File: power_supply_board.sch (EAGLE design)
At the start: 30 parts, among them J6 1744426-2

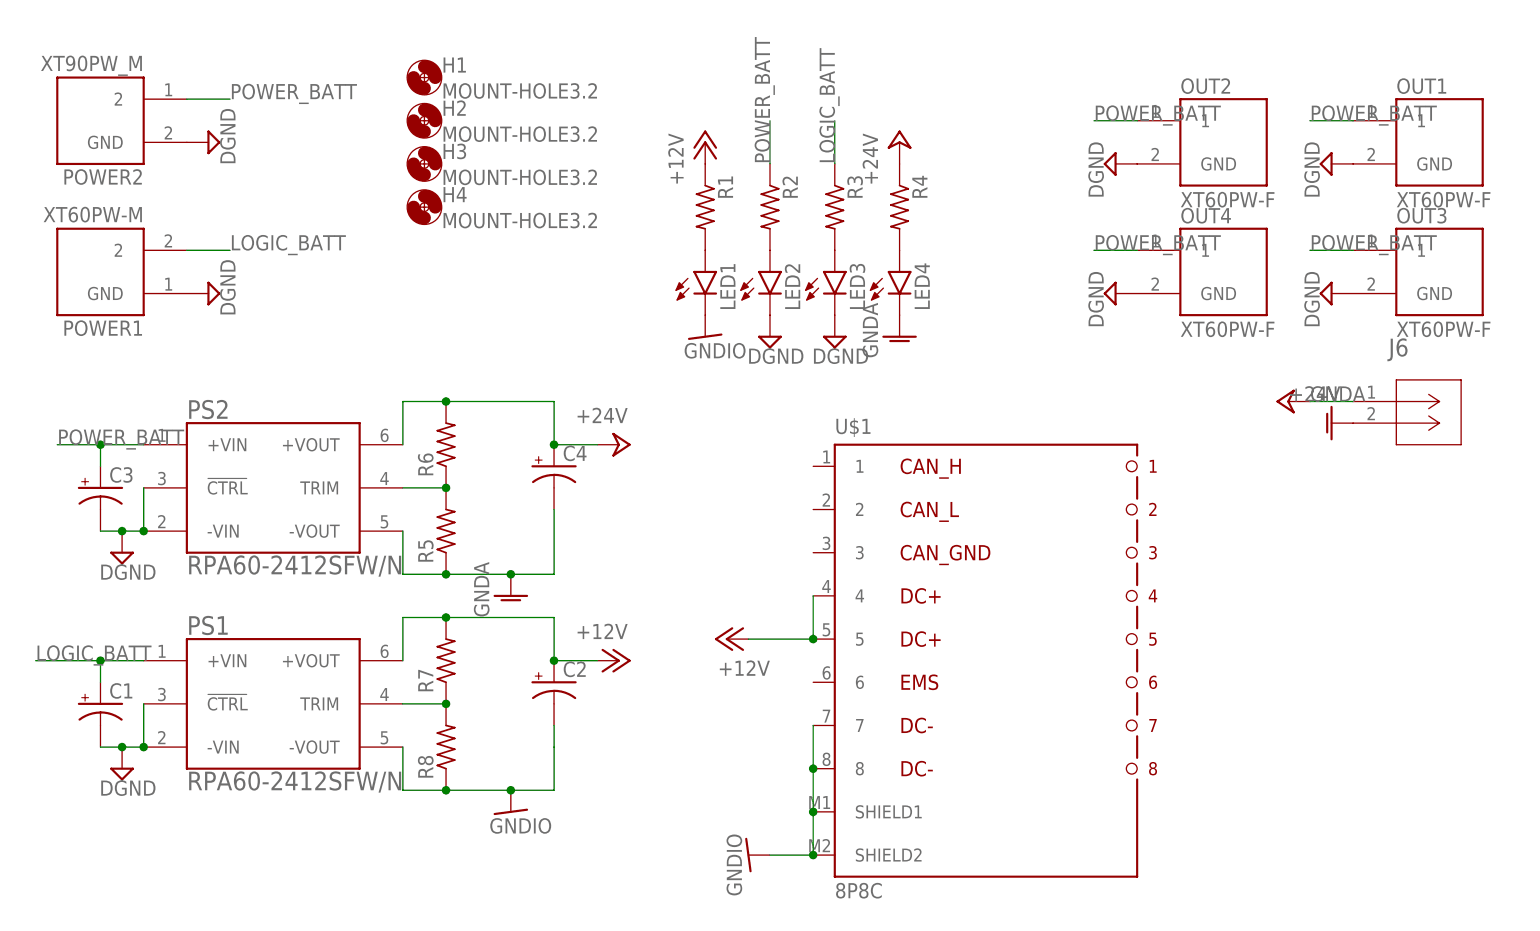
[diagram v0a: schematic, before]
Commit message: xt及びコンバータのthermalを外した
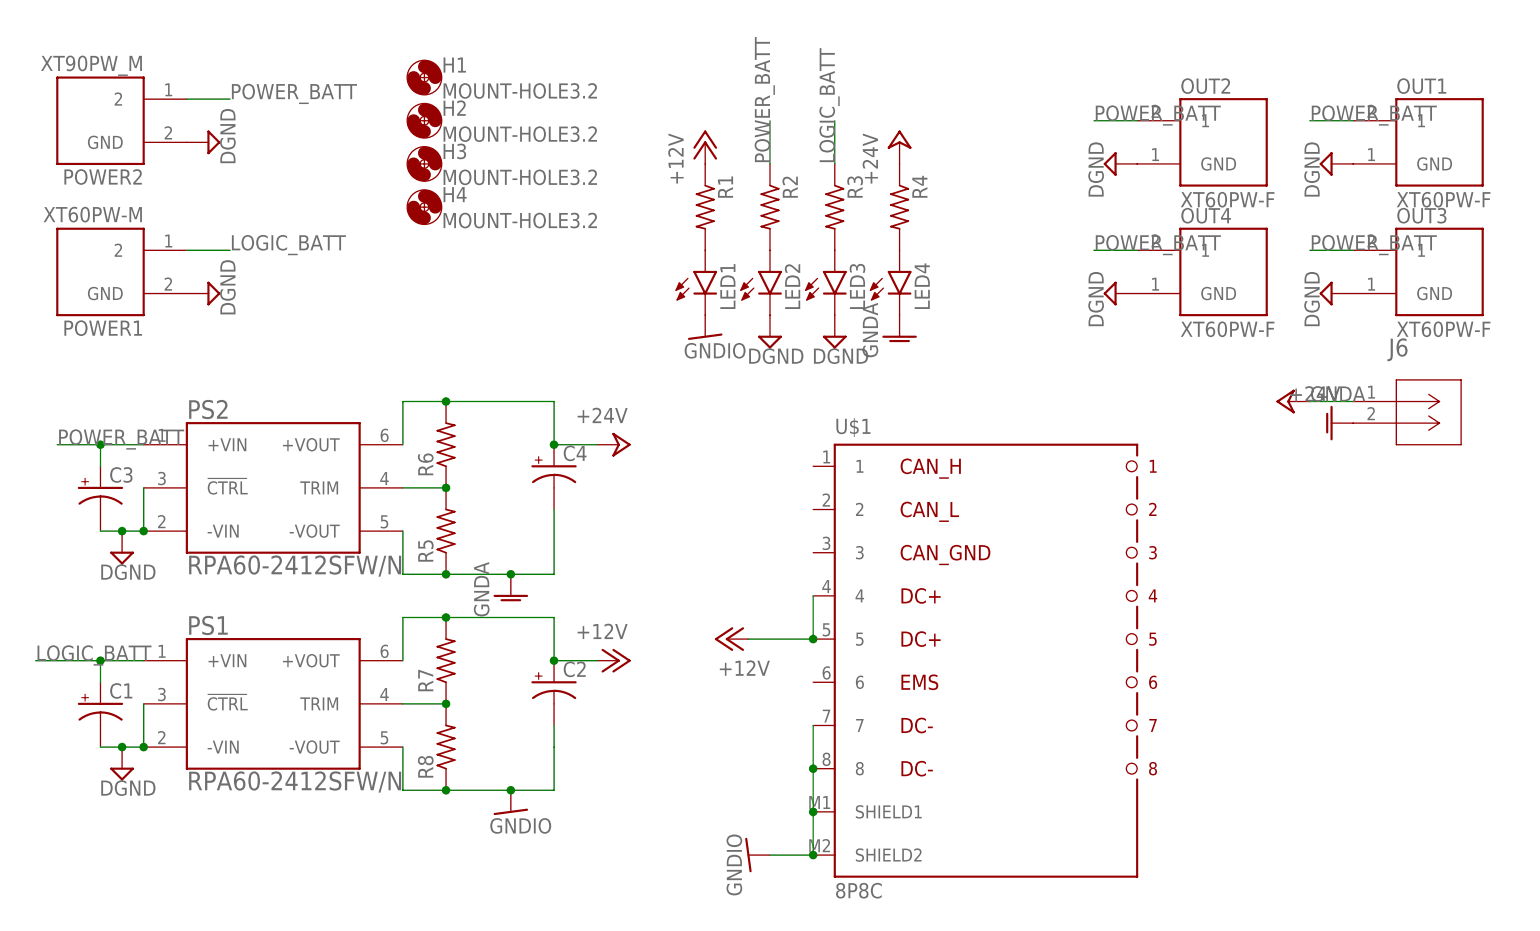
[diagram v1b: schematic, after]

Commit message: 配線ミスを修正
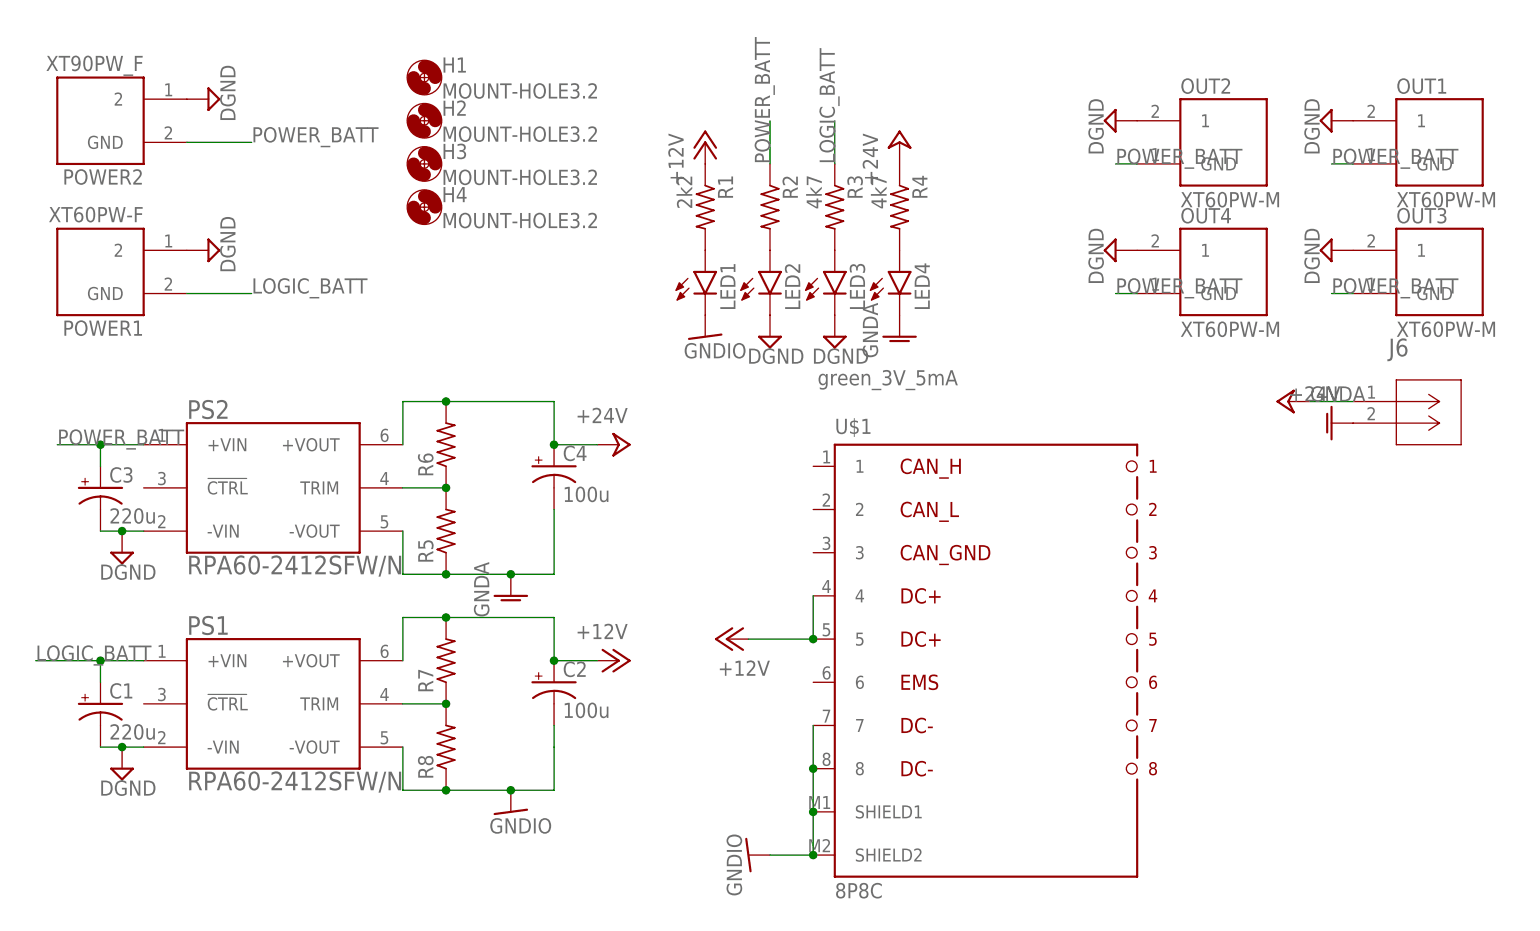
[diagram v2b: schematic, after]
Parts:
- C1, C3: value (none) -> 220u; device rcl:CPOL-USE2-5 -> rcl:CPOL-USE2.5-5
- C2, C4: value (none) -> 100u
- LED3: value (none) -> green_3V_5mA
- OUT1, OUT2, OUT3, OUT4: value XT60PW-F -> XT60PW-M; device XT60_Connecotr:XT60PW-F -> XT60_Connecotr:XT60PW-M
- POWER1: value XT60PW-M -> XT60PW-F; device XT60_Connecotr:XT60PW-M -> XT60_Connecotr:XT60PW-F
- POWER2: value XT90PW_M -> XT90PW_F; device XT60_Connecotr:XT90PW_M -> XT60_Connecotr:XT90PW_F
- R1: value (none) -> 2k2
- R3, R4: value (none) -> 4k7
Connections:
- net DGND: now also OUT1.1, OUT2.1, OUT3.1, OUT4.1, POWER1.2, POWER2.2; no longer OUT1.GND, OUT2.GND, OUT3.GND, OUT4.GND, POWER1.GND, POWER2.GND, PS1.!CTRL, PS2.!CTRL
- net LOGIC_BATT: now also POWER1.GND; no longer POWER1.2
- net POWER_BATT: now also OUT1.GND, OUT2.GND, OUT3.GND, OUT4.GND, POWER2.GND; no longer OUT1.1, OUT2.1, OUT3.1, OUT4.1, POWER2.2
